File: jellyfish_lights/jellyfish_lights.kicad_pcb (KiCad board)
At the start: 2 copper layers, 80 x 70.3 mm, 24 parts, among them Q1 AO3400A, SW1 tilt switch, U1 SN74LVC1G14DBV

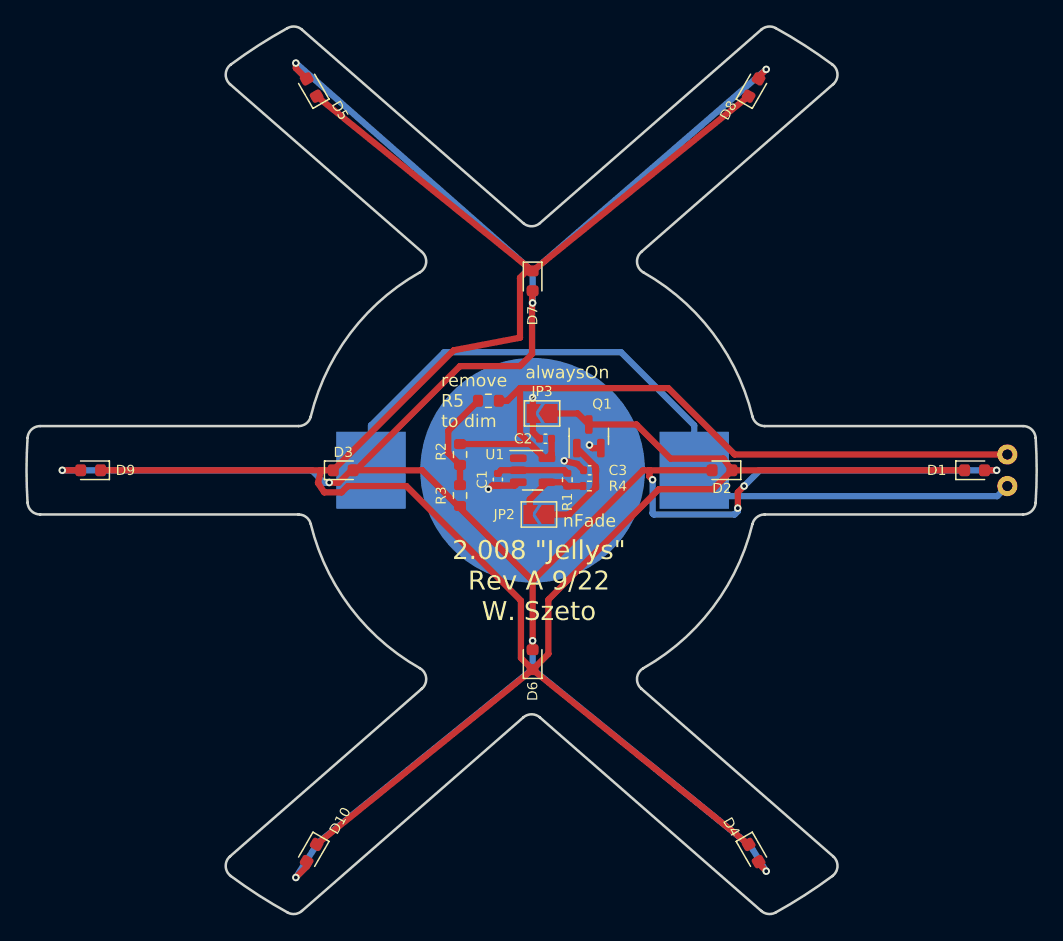
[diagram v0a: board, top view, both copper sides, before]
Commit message: Rev B01
Changed board shape
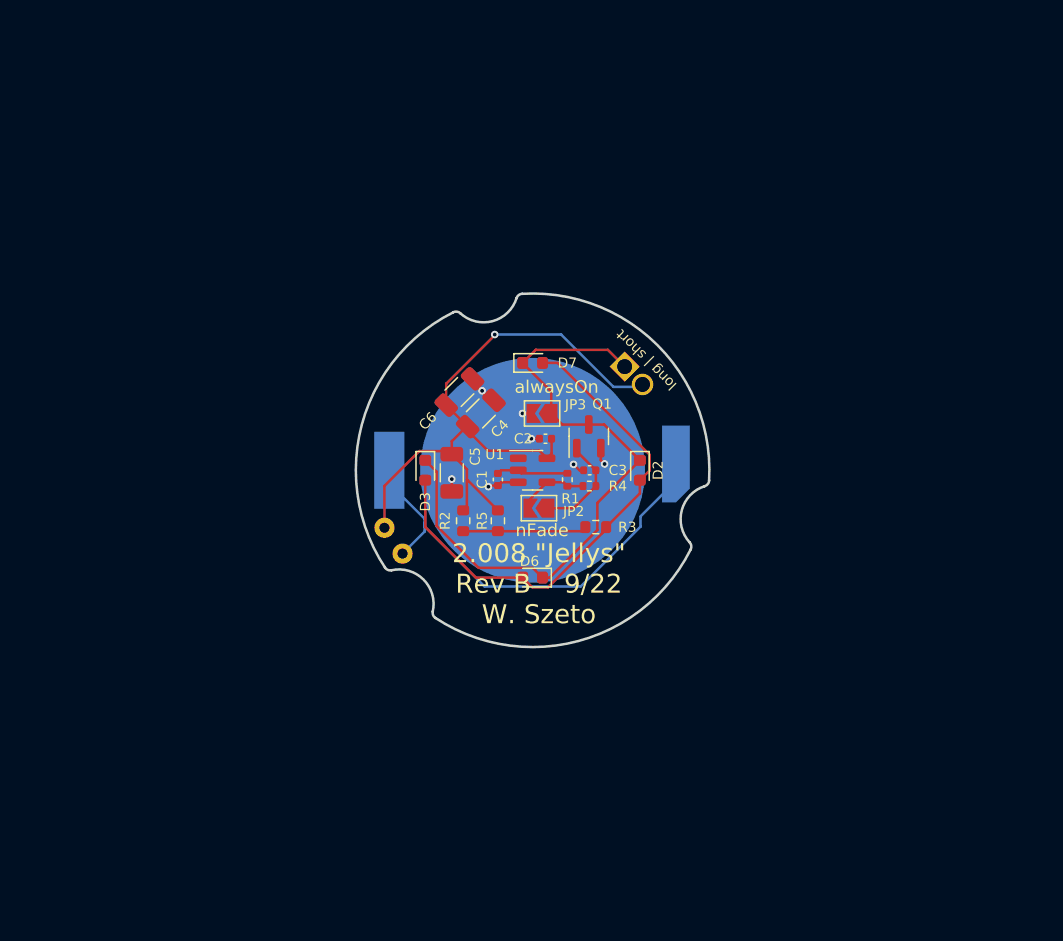
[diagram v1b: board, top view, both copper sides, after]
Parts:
- removed D10, D4, D5, D8, D9: LED, LED_SMD:LED_0603_1608Metric
- added C4: 100uF/6.3V, Capacitor_SMD:C_1206_3216Metric, F.Cu at (170.9, 100.5)
- added C5: 100uF/6.3V, Capacitor_SMD:C_1206_3216Metric, F.Cu at (168.6, 105.2)
- added C6: 100uF/6.3V, Capacitor_SMD:C_1206_3216Metric, F.Cu at (169.2, 98.8)
- C3: value 1uF -> 4.7uF
- D1: value LED -> 3mm THT LED; footprint LED_SMD:LED_0603_1608Metric -> LED_THT:LED_D5.0mm_FlatTop; moved to B.Cu
- D2, D3, D6, D7: value LED -> NCD0603W1
- R2: value 10R -> 0R
- R4: value 100K -> 330k
- R5: value 0R -> 10R
- U1: value SN74LVC1G14DBV -> SN74LVC1G14DBVR
- moved SW1 48.5 mm to (164.7, 111.6), turned to 125 degrees
- moved D1 29.1 mm to (182.1, 96.6), turned to -45 degrees
- moved R3 11.0 mm to (180.0, 109.5), turned to 0 degrees
- moved R5 9.53 mm to (172.2, 109.0), turned to -90 degrees
- moved D2 6.50 mm to (183.5, 105.0), turned to -90 degrees
- moved D3 6.50 mm to (166.5, 105.0), turned to -90 degrees
- moved D6 6.50 mm to (175.0, 113.5), turned to 180 degrees
- moved D7 6.50 mm to (175.0, 96.5), turned to 0 degrees
- moved R2 5.26 mm to (169.5, 109.0), turned to 90 degrees
- moved JP2 0.50 mm to (175.5, 108.0)
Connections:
- net Net-(D1-Pad1) renamed /LED-
- D1 pad 2: Net-(D1-Pad2) -> VCC
- D2 pad 2: Net-(D1-Pad2) -> /LED+
- D3 pad 2: Net-(D1-Pad2) -> /LED+
- D6 pad 2: Net-(D1-Pad2) -> /LED+
- D7 pad 2: Net-(D1-Pad2) -> /LED+
- R2 pad 1: VCC -> Net-(R2-Pad1)
- R2 pad 2: Net-(R2-Pad2) -> VCC
- R3 pad 1: Net-(R2-Pad2) -> Net-(R2-Pad1)
- R3 pad 2: Net-(D1-Pad2) -> /LED+
- R5 pad 2: Net-(R2-Pad2) -> Net-(R2-Pad1)
- SW1 pad 1: VCC -> Net-(BT1-Pad1)
- SW1 pad 2: Net-(BT1-Pad1) -> VCC
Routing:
- net Net-(D1-Pad2): track 232.7 -> 0.00 mm, vias 12 -> 0
- net /LED-: track 218.1 -> 50.7 mm
- net /LED+: track 0.00 -> 40.7 mm
- net Net-(BT1-Pad1): track 63.5 -> 35.4 mm
- net Net-(R2-Pad1): track 0.00 -> 9.81 mm
- net Net-(R2-Pad2): track 8.04 -> 0.00 mm
- net VCC: track 57.4 -> 53.3 mm, vias 0 -> 1
- net GND: track 8.83 -> 9.78 mm, vias 4 -> 7
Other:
- board size 80 x 70.3 mm -> 28 x 28 mm
- board text added: "2.008 {dblquote}Jellys{dblquote} Rev B 9/22 W. Szeto"
- board text added: "long"
- board text added: "long | short"
- board text added: "short"
- board text removed: "2.008 {dblquote}Jellys{dblquote} Rev A 9/22 W. Szeto"
- board text removed: "remove R5 to dim"

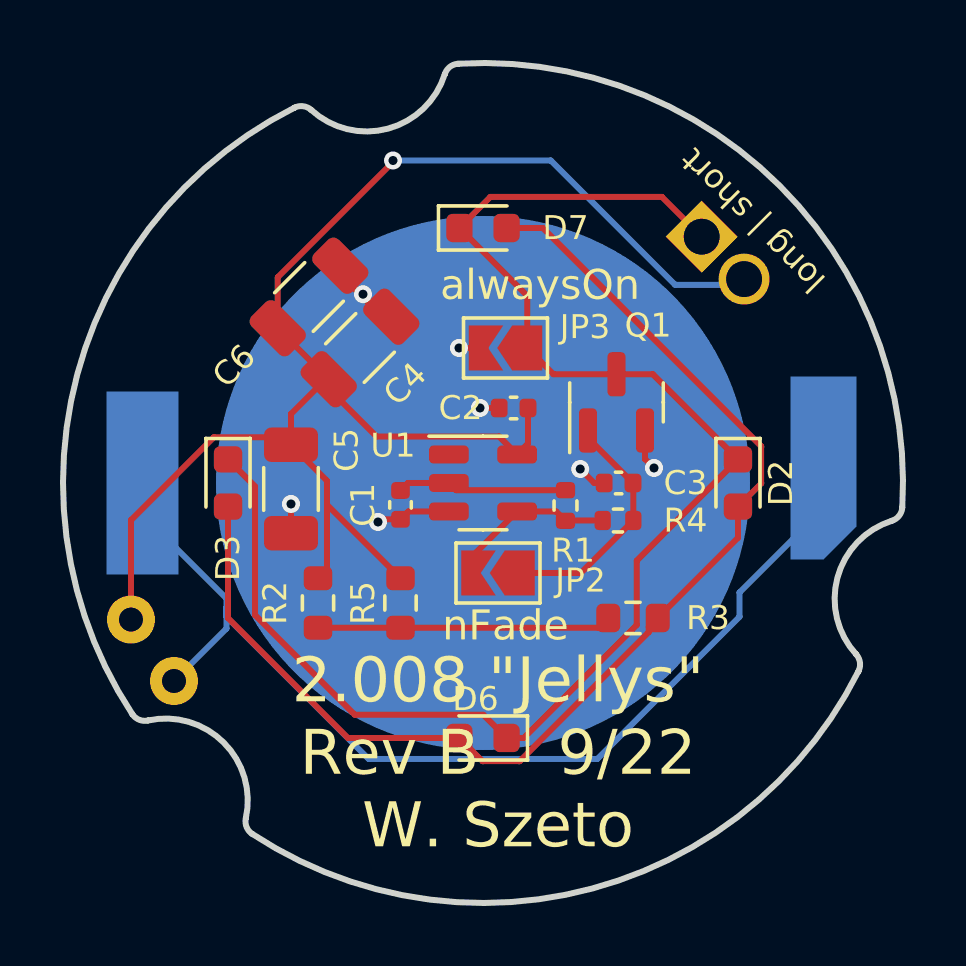
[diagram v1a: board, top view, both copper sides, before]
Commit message: Rev C01
-Edited THT footprints to accommodate easier soldering (moved away from BT1)
-Added SW2 to prevent turn-on events while not spinning
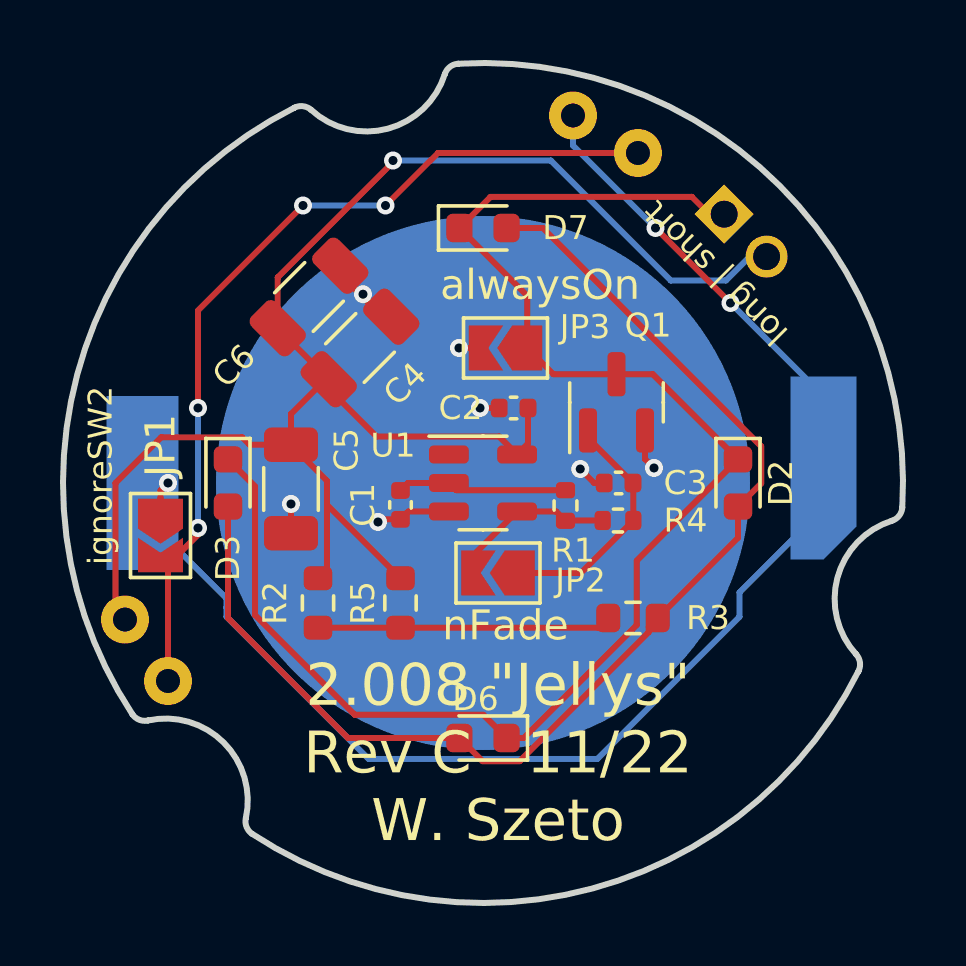
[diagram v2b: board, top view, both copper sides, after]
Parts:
- added JP1: oneTiltSw, Jumper:SolderJumper-2_P1.3mm_Open_TrianglePad1.0x1.5mm, F.Cu at (164.2, 106.8)
- added SW2: tilt switch, WS_LCSC_Mechanical:tilt_switch, B.Cu at (178.0, 92.8)
- moved D1 1.06 mm to (182.8, 95.8)
- moved SW1 0.20 mm to (164.5, 111.6)
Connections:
- SW1 pad 1: Net-(BT1-Pad1) -> Net-(SW1-Pad1)
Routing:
- net Net-(SW1-Pad1): track 0.00 -> 29.8 mm, vias 0 -> 4
- net Net-(BT1-Pad1): track 35.4 -> 48.6 mm, vias 0 -> 3
- net VCC: track 53.3 -> 55.0 mm
- net /LED-: track 50.7 -> 51.3 mm
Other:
- board text added: "2.008 {dblquote}Jellys{dblquote} Rev C 11/22 W. Szeto"
- board text added: "ignoreSW2"
- board text removed: "2.008 {dblquote}Jellys{dblquote} Rev B 9/22 W. Szeto"
- board text removed: "short"

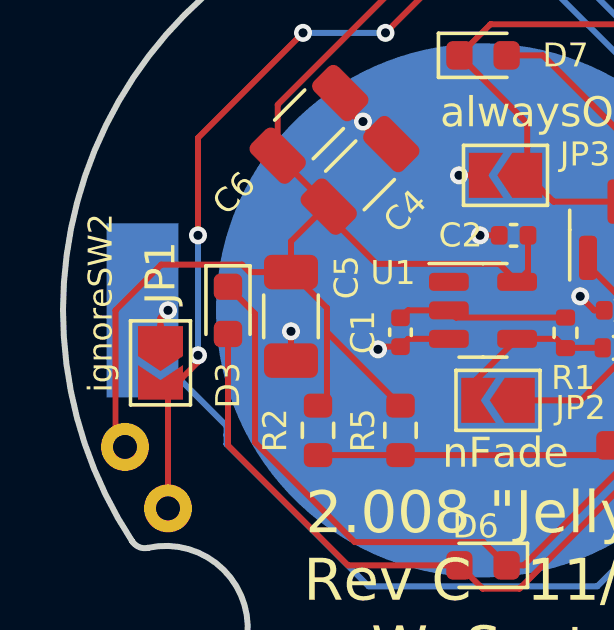
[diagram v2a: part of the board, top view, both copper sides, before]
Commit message: changed jumper to 0R resistor for ignoreSW2
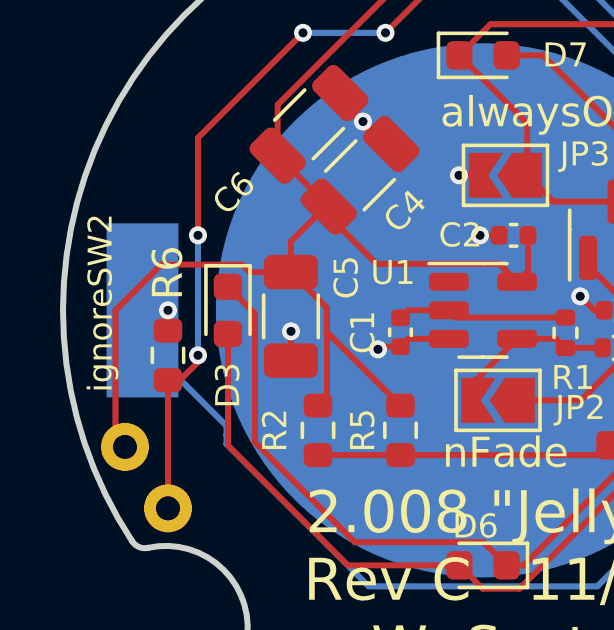
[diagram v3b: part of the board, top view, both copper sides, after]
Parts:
- removed JP1: oneTiltSw, Jumper:SolderJumper-2_P1.3mm_Open_TrianglePad1.0x1.5mm
- added R6: 0R, Resistor_SMD:R_0603_1608Metric, F.Cu at (164.5, 106.5)
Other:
- board text added: "Rev C"
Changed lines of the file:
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@@
     (descr "Capacitor SMD 0402 (1005 Metric), square (rectangular) end terminal, IPC_7351 nominal, (Body size source: IPC-SM-782 page 76, https://www.pcb-3d.com/wordpress/wp-content/uploads/ipc-sm-782a_amendment_1_and_2.pdf), generated with kicad-footprint-generator")
     (tags "capacitor")
-    (property "LCSC" "C1525")
+    (property "LCSC" "")
     (property "Sheetfile" "jellyfish_lights.kicad_sch")
     (property "Sheetname" "")
@@
     )
   )
-  (footprint "Jumper:SolderJumper-2_P1.3mm_Open_TrianglePad1.0x1.5mm" (layer "F.Cu")
-    (at 164.25 106.75 -90)
-    (descr "SMD Solder Jumper, 1x1.5mm Triangular Pads, 0.3mm gap, open")
-    (tags "solder jumper open")
-    (property "Sheetfile" "jellyfish_lights.kicad_sch")
-    (property "Sheetname" "")
-    (attr exclude_from_pos_files)
-    (fp_text reference "JP1" (at -3 0 90) (layer "F.SilkS")
-      (effects (font (size 1 1) (thickness 0.15)))
-    )
-    (fp_text value "oneTiltSw" (at 0 1.9 90) (layer "F.Fab")
-      (effects (font (size 1 1) (thickness 0.15)))
-    )
-    (fp_line (start -1.4 1) (end -1.4 -1) (layer "F.SilkS") (width 0.12))
-    (fp_line (start 1.4 1) (end -1.4 1) (layer "F.SilkS") (width 0.12))
-    (fp_line (start 1.4 -1) (end 1.4 1) (layer "F.SilkS") (width 0.12))
-    (fp_line (start -1.4 -1) (end 1.4 -1) (layer "F.SilkS") (width 0.12))
-    (fp_line (start 1.65 1.25) (end -1.65 1.25) (layer "F.CrtYd") (width 0.05))
-    (fp_line (start -1.65 -1.25) (end 1.65 -1.25) (layer "F.CrtYd") (width 0.05))
-    (fp_line (start 1.65 1.25) (end 1.65 -1.25) (layer "F.CrtYd") (width 0.05))
-    (fp_line (start -1.65 -1.25) (end -1.65 1.25) (layer "F.CrtYd") (width 0.05))
-    (pad "1" smd custom (at -0.725 0 270) (size 0.3 0.3) (layers "F.Cu" "F.Mask")
-      (net 1 "Net-(BT1-Pad1)") (pinfunction "A") (pintype "passive") (zone_connect 2)
-      (options (clearance outline) (anchor rect))
-      (primitives
-        (gr_poly (pts
-            (xy 1 0)
-            (xy 0.5 0.75)
-            (xy -0.5 0.75)
-            (xy -0.5 -0.75)
-            (xy 0.5 -0.75)
-          ) (width 0) (fill yes))
-      ))
-    (pad "2" smd custom (at 0.725 0 270) (size 0.3 0.3) (layers "F.Cu" "F.Mask")
-      (net 11 "Net-(SW1-Pad1)") (pinfunction "B") (pintype "passive") (zone_connect 2)
-      (options (clearance outline) (anchor rect))
-      (primitives
-        (gr_poly (pts
-            (xy 0.5 0.75)
-            (xy -0.65 0.75)
-            (xy -0.15 0)
-            (xy -0.65 -0.75)
-            (xy 0.5 -0.75)
-          ) (width 0) (fill yes))
-      ))
+  (footprint "Resistor_SMD:R_0603_1608Metric" (layer "F.Cu")
+    (at 164.5 106.5 -90)
+    (descr "Resistor SMD 0603 (1608 Metric), square (rectangular) end terminal, IPC_7351 nominal, (Body size source: IPC-SM-782 page 72, https://www.pcb-3d.com/wordpress/wp-content/uploads/ipc-sm-782a_amendment_1_and_2.pdf), generated with kicad-footprint-generator")
+    (tags "resistor")
+    (property "LCSC" "C21189")
+    (property "Sheetfile" "jellyfish_lights.kicad_sch")
+    (property "Sheetname" "")
+    (attr smd)
+    (fp_text reference "R6" (at -2.75 0 90) (layer "F.SilkS")
+      (effects (font (size 1 1) (thickness 0.15)))
+    )
+    (fp_text value "0R" (at 0 1.43 90) (layer "F.Fab")
+      (effects (font (size 1 1) (thickness 0.15)))
+    )
+    (fp_text user "${REFERENCE}" (at 0 0 90) (layer "F.Fab")
+      (effects (font (size 0.4 0.4) (thickness 0.06)))
+    )
+    (fp_line (start -0.237258 0.5225) (end 0.237258 0.5225) (layer "F.SilkS") (width 0.12))
+    (fp_line (start -0.237258 -0.5225) (end 0.237258 -0.5225) (layer "F.SilkS") (width 0.12))
+    (fp_line (start 1.48 -0.73) (end 1.48 0.73) (layer "F.CrtYd") (width 0.05))
+    (fp_line (start -1.48 0.73) (end -1.48 -0.73) (layer "F.CrtYd") (width 0.05))
+    (fp_line (start 1.48 0.73) (end -1.48 0.73) (layer "F.CrtYd") (width 0.05))
+    (fp_line (start -1.48 -0.73) (end 1.48 -0.73) (layer "F.CrtYd") (width 0.05))
+    (fp_line (start 0.8 0.4125) (end -0.8 0.4125) (layer "F.Fab") (width 0.1))
+    (fp_line (start -0.8 -0.4125) (end 0.8 -0.4125) (layer "F.Fab") (width 0.1))
+    (fp_line (start -0.8 0.4125) (end -0.8 -0.4125) (layer "F.Fab") (width 0.1))
+    (fp_line (start 0.8 -0.4125) (end 0.8 0.4125) (layer "F.Fab") (width 0.1))
+    (pad "1" smd roundrect (at -0.825 0 270) (size 0.8 0.95) (layers "F.Cu" "F.Paste" "F.Mask") (roundrect_rratio 0.25)
+      (net 1 "Net-(BT1-Pad1)") (pintype "passive"))
+    (pad "2" smd roundrect (at 0.825 0 270) (size 0.8 0.95) (layers "F.Cu" "F.Paste" "F.Mask") (roundrect_rratio 0.25)
+      (net 11 "Net-(SW1-Pad1)") (pintype "passive"))
+    (model "${KICAD6_3DMODEL_DIR}/Resistor_SMD.3dshapes/R_0603_1608Metric.wrl"
+      (offset (xyz 0 0 0))
+      (scale (xyz 1 1 1))
+      (rotate (xyz 0 0 0))
+    )
   )
   (footprint "Resistor_SMD:R_0603_1608Metric" (layer "F.Cu")
@@
   (gr_arc (start 167.308417 116.697842) (mid 167.11995 116.468415) (end 167.094807 116.17257) (layer "Edge.Cuts") (width 0.2))
   (gr_arc (start 163.835037 112.915933) (mid 166.357178 113.651137) (end 167.094807 116.17257) (layer "Edge.Cuts") (width 0.2))
+  (gr_text "Rev C" (at 174.75 118) (layer "B.SilkS")
+    (effects (font (size 1 1) (thickness 0.15)) (justify mirror))
+  )
   (gr_text "CR2032" (at 175.3 116.3) (layer "B.SilkS")
     (effects (font (size 1 1) (thickness 0.2)) (justify mirror))
@@
   )
   (segment (start 183.25 99) (end 180.75 96.5) (width 0.2) (layer "F.Cu") (net 1))
-  (segment (start 164.25 105.5) (end 164.25 105.25) (width 0.2) (layer "F.Cu") (net 1))
-  (segment (start 164.25 106.025) (end 164.25 105.5) (width 0.2) (layer "F.Cu") (net 1))
-  (segment (start 164.25 105.25) (end 164.5 105) (width 0.2) (layer "F.Cu") (net 1))
+  (segment (start 164.5 105) (end 164.5 105.675) (width 0.2) (layer "F.Cu") (net 1))
   (via (at 164.5 105) (size 0.6) (drill 0.3) (layers "F.Cu" "B.Cu") (net 1))
   (via (at 180.75 96.5) (size 0.6) (drill 0.3) (layers "F.Cu" "B.Cu") (net 1))

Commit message: fixing LCSC numbers
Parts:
- C4, C5, C6: value 100uF/6.3V -> DNP
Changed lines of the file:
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@@
       (effects (font (size 0.8 0.8) (thickness 0.15)))
     )
-    (fp_text value "100uF/6.3V" (at 0 1.85 90) (layer "F.Fab")
+    (fp_text value "DNP" (at 0 1.85 90) (layer "F.Fab")
       (effects (font (size 1 1) (thickness 0.15)))
     )
@@
       (effects (font (size 0.8 0.8) (thickness 0.15)))
     )
-    (fp_text value "100uF/6.3V" (at 0 1.85 45) (layer "F.Fab")
+    (fp_text value "DNP" (at 0 1.85 45) (layer "F.Fab")
       (effects (font (size 1 1) (thickness 0.15)))
     )
@@
     (descr "Capacitor SMD 0402 (1005 Metric), square (rectangular) end terminal, IPC_7351 nominal, (Body size source: IPC-SM-782 page 76, https://www.pcb-3d.com/wordpress/wp-content/uploads/ipc-sm-782a_amendment_1_and_2.pdf), generated with kicad-footprint-generator")
     (tags "capacitor")
-    (property "LCSC" "C1525")
+    (property "LCSC" "C23733")
     (property "Sheetfile" "jellyfish_lights.kicad_sch")
     (property "Sheetname" "")
@@
       (effects (font (size 0.8 0.8) (thickness 0.15)))
     )
-    (fp_text value "100uF/6.3V" (at 0 1.85 45) (layer "F.Fab")
-      (effects (font (size 1 1) (thickness 0.15)))
-    )
+    (fp_text value "DNP" (at 0 1.85 45) (layer "F.Fab")
+      (effects (font (size 1 1) (thickness 0.15)))
+    )
